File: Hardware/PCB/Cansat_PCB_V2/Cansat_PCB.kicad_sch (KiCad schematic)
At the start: 50 parts, among them J1 Lecteur SD, SW1 RSTBTN, SW2 boot, U1 Barometre BMP581, U2 STM32G431CBUx, U3 IMU BNO055, Y1 Crystal_GND24_Small, Y2 Oscillateur_IMU

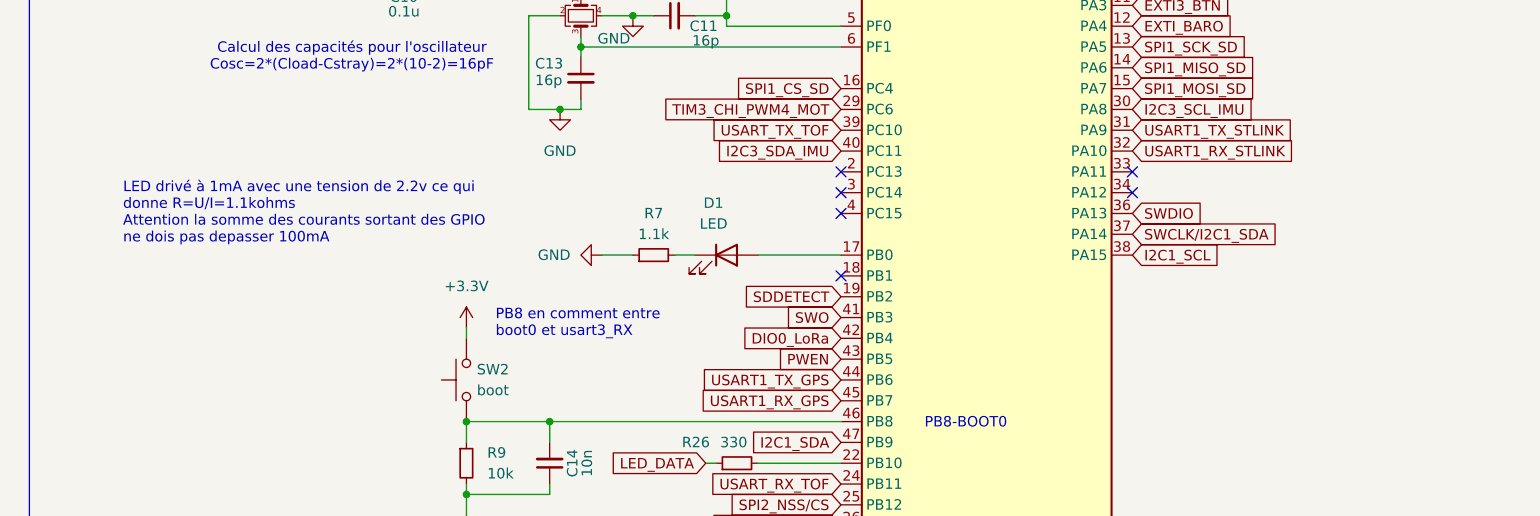
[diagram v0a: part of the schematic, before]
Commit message: Conn Camera 2 pins et deplacement du transistor dans un pcb intermédiaire
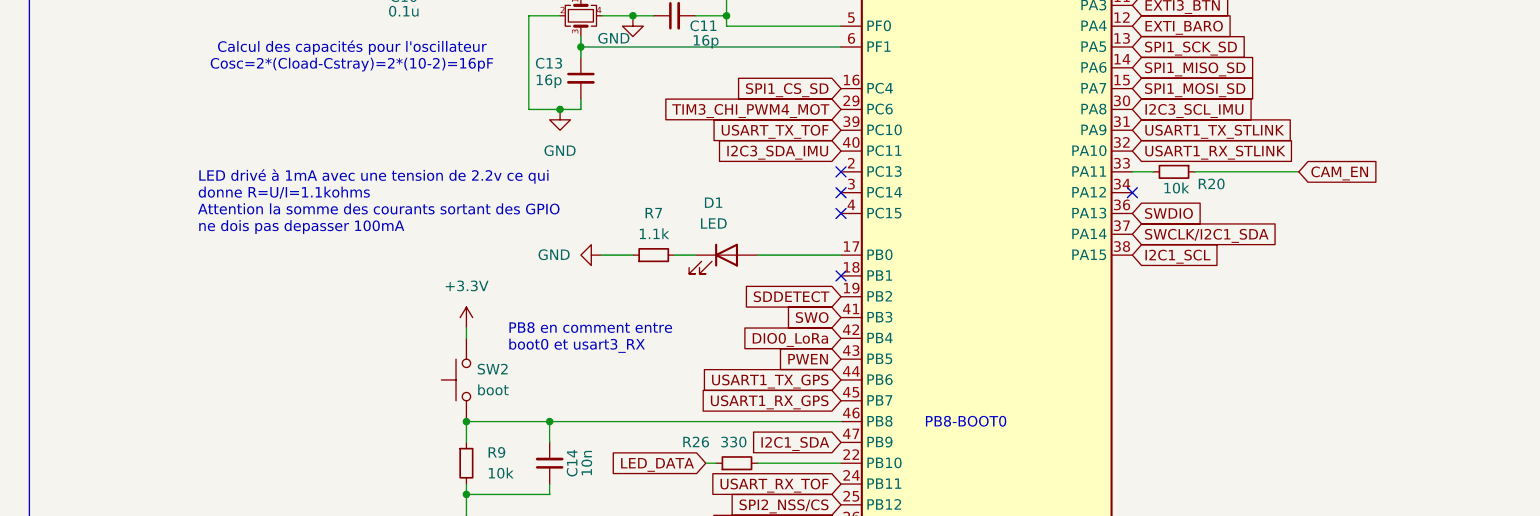
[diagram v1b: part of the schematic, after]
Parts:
- added R20: 10k, Resistor_SMD:R_0402_1005Metric_Pad0.72x0.64mm_HandSolder, symbol Device:R_Small
- Y1: footprint footprints:SMD3225_3.2X2.5X0.7_MTC -> footprints:Crystal_SMD_3225-4pin_3.2x2.5mm
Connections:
- net at U2.33 (PA11): now also R20.2
- new net CAM_EN: R20.1
- no-connect marks 12 -> 11
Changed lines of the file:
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@@
 	(text "PB8 en comment entre \nboot0 et usart3_RX"
 		(exclude_from_sim no)
-		(at 74.676 112.522 0)
+		(at 76.2 114.3 0)
 		(effects
 			(font
@@
 	(text "LED drivé à 1mA avec une tension de 2.2v ce qui \ndonne R=U/I=1.1kohms\nAttention la somme des courants sortant des GPIO \nne dois pas depasser 100mA"
 		(exclude_from_sim no)
-		(at 29.21 99.06 0)
+		(at 38.354 97.79 0)
 		(effects
 			(font
@@
 	)
 	(no_connect
-		(at 152.4 93.98)
-	)
-	(no_connect
 		(at 88.9 189.23)
 	)
@@
 	)
 	(no_connect
+		(at 116.84 106.68)
+	)
+	(no_connect
 		(at 88.9 207.01)
 	)
@@
 		(at 116.84 93.98)
 	)
-	(no_connect
-		(at 116.84 106.68)
-	)
 	(wire
 		(pts
@@
 	(wire
 		(pts
+			(xy 152.4 93.98) (xy 154.94 93.98)
+		)
+		(stroke
+			(width 0)
+			(type default)
+		)
+	)
+	(wire
+		(pts
 			(xy 290.83 160.02) (xy 290.83 181.61)
 		)
@@
 	(wire
 		(pts
+			(xy 172.72 93.98) (xy 160.02 93.98)
+		)
+		(stroke
+			(width 0)
+			(type default)
+		)
+	)
+	(wire
+		(pts
 			(xy 176.53 52.07) (xy 176.53 50.8)
 		)
@@
 		)
 	)
+	(global_label "CAM_EN"
+		(shape input)
+		(at 172.72 93.98 0)
+		(fields_autoplaced yes)
+		(effects
+			(font
+				(size 1.27 1.27)
+			)
+			(justify left)
+		)
+		(property "Intersheetrefs" "${INTERSHEET_REFS}"
+			(at 182.9623 93.98 0)
+			(effects
+				(font
+					(size 1.27 1.27)
+				)
+				(justify left)
+				(hide yes)
+			)
+		)
+	)
 	(global_label "TIM3_CHI_PWM4_MOT"
 		(shape input)
@@
 	)
 	(symbol
+		(lib_id "Device:R_Small")
+		(at 157.48 93.98 270)
+		(unit 1)
+		(exclude_from_sim no)
+		(in_bom yes)
+		(on_board yes)
+		(dnp no)
+		(property "Reference" "R20"
+			(at 162.052 95.504 90)
+			(effects
+				(font
+					(size 1.27 1.27)
+				)
+			)
+		)
+		(property "Value" "10k"
+			(at 157.734 96.012 90)
+			(effects
+				(font
+					(size 1.27 1.27)
+				)
+			)
+		)
+		(property "Footprint" "Resistor_SMD:R_0402_1005Metric_Pad0.72x0.64mm_HandSolder"
+			(at 157.48 93.98 0)
+			(effects
+				(font
+					(size 1.27 1.27)
+				)
+				(hide yes)
+			)
+		)
+		(property "Datasheet" "~"
+			(at 157.48 93.98 0)
+			(effects
+				(font
+					(size 1.27 1.27)
+				)
+				(hide yes)
+			)
+		)
+		(property "Description" "Resistor, small symbol"
+			(at 157.48 93.98 0)
+			(effects
+				(font
+					(size 1.27 1.27)
+				)
+				(hide yes)
+			)
+		)
+		(pin "1"
+		)
+		(pin "2"
+		)
+		(instances
+			(project "Cansat_PCB"
+				(path "/43b9f51a-edfb-48c9-aab9-a28c7efe9297"
+					(reference "R20")
+					(unit 1)
+				)
+			)
+		)
+	)
+	(symbol
 		(lib_id "power:GND")
 		(at 134.62 152.4 0)
@@
 			)
 		)
-		(property "Footprint" "footprints:SMD3225_3.2X2.5X0.7_MTC"
+		(property "Footprint" "footprints:Crystal_SMD_3225-4pin_3.2x2.5mm"
 			(at 85.09 74.93 0)
 			(effects
